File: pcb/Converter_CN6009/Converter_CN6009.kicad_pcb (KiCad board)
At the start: 2 copper layers, 45 x 22.5 mm, 15 parts, among them J1 IN+, J2 IN-, J3 OUT+, J4 OUT-

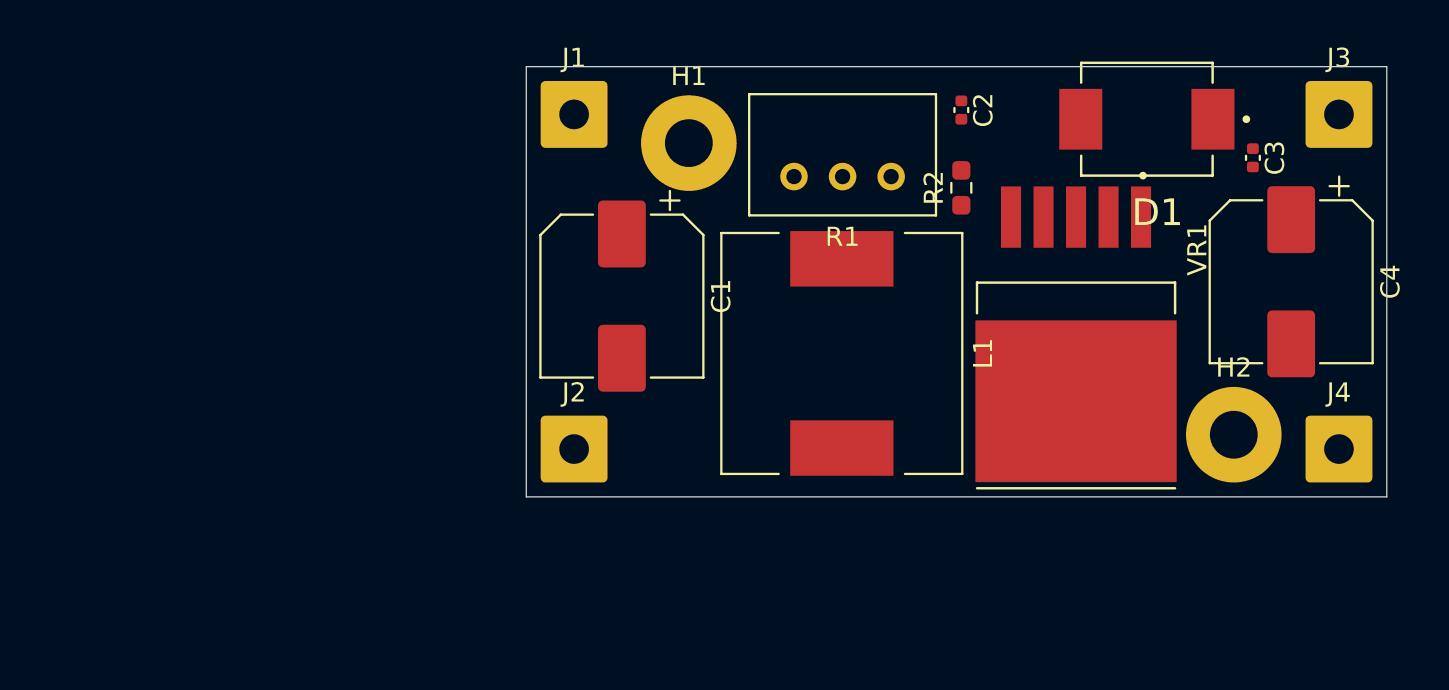
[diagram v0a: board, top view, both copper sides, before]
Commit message: se realizo ruteo de pcb y correciones
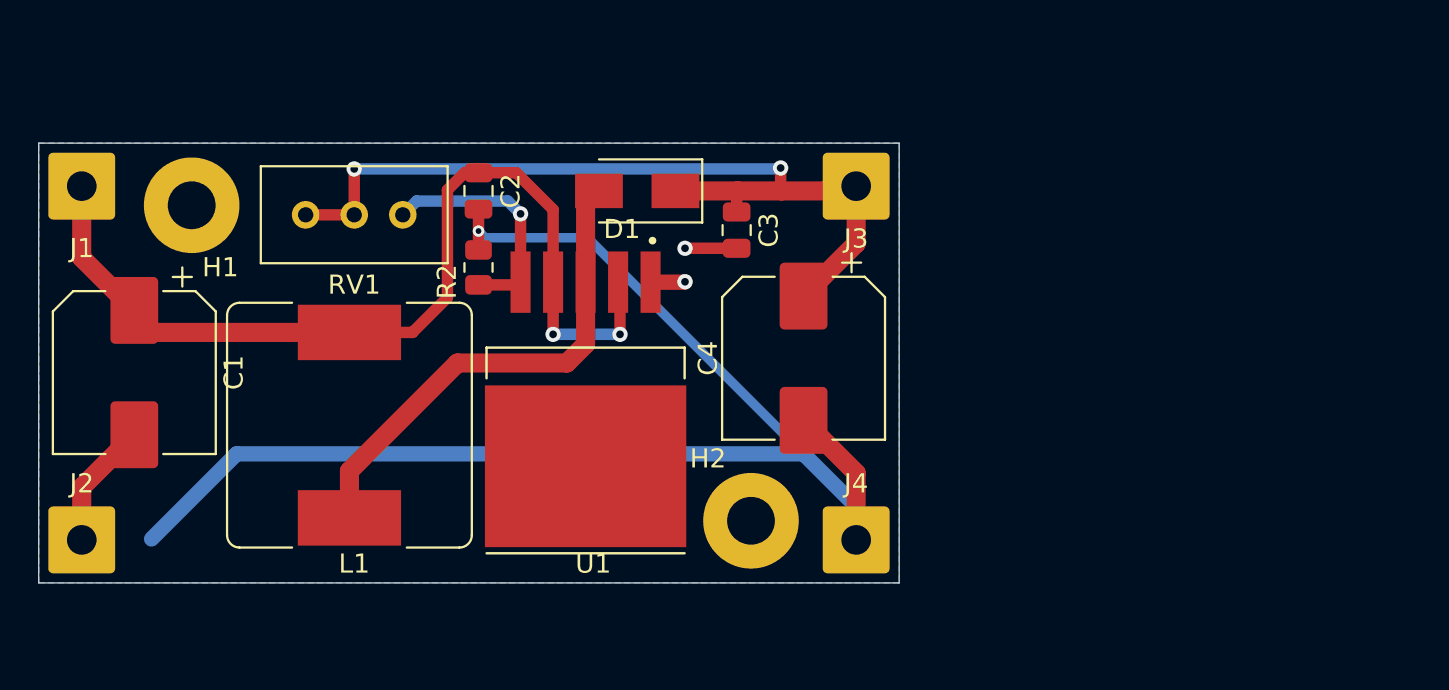
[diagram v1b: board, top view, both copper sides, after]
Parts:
- removed R1: 50K, Potentiometer_THT:Potentiometer_Bourns_3299W_Vertical
- added RV1: R_POT_TRIM, Potentiometer_THT:Potentiometer_Bourns_3296W_Vertical, F.Cu at (119.5, 88.2)
- C2, C3: footprint Capacitor_SMD:C_0402_1005Metric -> Capacitor_SMD:C_0805_2012Metric
- D1: value SS34 -> D_Schottky; footprint SS34:DIOM7959X265N -> Diode_SMD:D_SMA
- L1: footprint Inductor_SMD:L_12x12mm_H8mm -> Inductor_SMD:L_Bourns_SRR1260
- R2: footprint Resistor_SMD:R_0603_1608Metric_Pad0.98x0.95mm_HandSolder -> Resistor_SMD:R_0805_2012Metric
- moved C3 27.3 mm to (142.0, 89.0)
- moved D1 26.9 mm to (136.8, 87.0)
- moved H1 26.2 mm to (113.5, 87.8)
- moved J2 26.2 mm to (107.8, 105.2)
- moved J1 26.0 mm to (107.8, 86.8)
- moved L1 26.0 mm to (121.8, 99.2)
- moved U1 25.9 mm to (134.1, 97.9)
- moved C1 25.8 mm to (110.5, 96.5)
- moved C4 25.8 mm to (145.5, 95.8)
- moved J4 25.7 mm to (148.2, 105.2)
- moved H2 25.6 mm to (142.8, 104.2)
- moved C2 25.6 mm to (128.5, 87.0)
- moved R2 25.6 mm to (128.5, 91.0)
- moved J3 25.5 mm to (148.2, 86.8)
- renumbered VR1 to U1
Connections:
- L1 pad 2: Net-(D1-PadA) -> Net-(D1-Pad2)
- U1 pad 3: Net-(D1-PadA) -> Net-(D1-Pad2)
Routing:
- net GND: track 0.00 -> 88.0 mm, vias 0 -> 3
- net Net-(C1-Pad1): track 0.00 -> 51.0 mm, vias 0 -> 2
- net Net-(C3-Pad1): track 0.41 -> 47.4 mm, vias 0 -> 2
- net Net-(D1-Pad2): track 0.00 -> 26.2 mm
- net Net-(R2-Pad1): track 0.00 -> 12.7 mm, vias 0 -> 1
- added copper zone on B.Cu, net GND
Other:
- board size 45 x 22.5 mm -> 45 x 23 mm
- net class Default: clearance 0.8 -> 0.6
- rule trace_clearance: 0.8 -> 0.6
- board text added: "* 0,3mm agujero de via"
- board text added: "* 0,4 mm agujero de via"
- board text added: "* 0,5mm para posicionamiento de PCB"
- board text added: "* 0,6 mm pad de via"
- board text added: "* 0,6mm de margen"
- board text added: "* 0,8mm pad de via"
- board text added: "* 1mm para contorno de PCB"
- board text added: "* 1mm y 0,6mm de ancho de pista"
- board text added: "* Bottom : B.Cu"
- board text added: "* Top : F.Cu"
- board text added: "<----------- CN6009"
- board text added: "Capas"
- board text added: "DCI-FIUBA"
- board text added: "Grilla"
- board text added: "IN+"
- board text added: "IN-"
- board text added: "OUT+"
- board text added: "OUT-"
- board text added: "Replica Conversor DC-DC CN6009"
- board text added: "Tamaños seleccionados"

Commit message: se realizo todas las correcciones para la revision final
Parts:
- removed J1: IN+, Connector_Wire:SolderWire-0.75sqmm_1x01_D1.25mm_OD3.5mm
- removed J2: IN-, Connector_Wire:SolderWire-0.75sqmm_1x01_D1.25mm_OD3.5mm
- removed J3: OUT+, Connector_Wire:SolderWire-0.75sqmm_1x01_D1.25mm_OD3.5mm
- removed J4: OUT-, Connector_Wire:SolderWire-0.75sqmm_1x01_D1.25mm_OD3.5mm
- added FID1: Fiducial, Fiducial:Fiducial_0.75mm_Mask1.5mm, F.Cu at (114.2, 107.0)
- added IN+: J1, Connector_Wire:SolderWire-0.75sqmm_1x01_D1.25mm_OD3.5mm, F.Cu at (110.5, 90.5)
- added IN-: J2, Connector_Wire:SolderWire-0.75sqmm_1x01_D1.25mm_OD3.5mm, F.Cu at (110.5, 108.5)
- added OUT+: J3, Connector_Wire:SolderWire-0.75sqmm_1x01_D1.25mm_OD3.5mm, F.Cu at (150.5, 90.5)
- added OUT-: J4, Connector_Wire:SolderWire-0.75sqmm_1x01_D1.25mm_OD3.5mm, F.Cu at (150.5, 108.5)
- D1: value D_Schottky -> SS34
- RV1: value R_POT_TRIM -> 50K
- moved H1 4.45 mm to (116.2, 91.2)
- moved C1 4.30 mm to (113.0, 100.0)
- moved C2 4.30 mm to (131.0, 90.5)
- moved C3 4.30 mm to (144.5, 92.5)
- moved C4 4.30 mm to (148.0, 99.2)
- moved D1 4.30 mm to (139.3, 90.5)
- moved H2 4.30 mm to (145.2, 107.8)
- moved L1 4.30 mm to (124.2, 102.8)
- moved R2 4.30 mm to (131.0, 94.5)
- moved RV1 4.30 mm to (122.0, 91.8)
- moved U1 4.30 mm to (136.6, 101.4)
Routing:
- net GND: track 88.0 -> 72.3 mm, vias 3 -> 4
- net Net-(C3-Pad1): track 47.4 -> 45.9 mm
- added copper zone on F.Cu, net GND
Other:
- board text added: "* 0,5 mm agujero de via"
- board text added: "* 0,5 mm para posicionamiento de PCB"
- board text added: "* 0,6 mm de margen"
- board text added: "* 1 mm pad de via"
- board text added: "* 1 mm para contorno de PCB"
- board text added: "* 1mm y 0,6 mm de ancho de pista"
- board text added: "* 23 mm de ancho"
- board text added: "* 45 mm de largo"
- board text added: "Conversor DC/DC Step-Up Ajustable"
- board text added: "Diseñado en Argentina"
- board text added: "Diseño referenciado en el fabricante XLSEMI"
- board text added: "FIUBA-DCI"
- board text added: "Grilla:"
- board text added: "Tamaño de PCB:"
- board text added: "Tamaños seleccionados:"
- board text added: "Terminacion Superficial: HASL sin plomo"
- board text removed: "* 0,3mm agujero de via"
- board text removed: "* 0,4 mm agujero de via"
- board text removed: "* 0,5mm para posicionamiento de PCB"
- board text removed: "* 0,6 mm pad de via"
- board text removed: "* 0,6mm de margen"
- board text removed: "* 0,8mm pad de via"
- board text removed: "* 1mm para contorno de PCB"
- board text removed: "* 1mm y 0,6mm de ancho de pista"
- board text removed: "DCI-FIUBA"
- board text removed: "Grilla"
- board text removed: "Replica Conversor DC-DC CN6009"
- board text removed: "Tamaños seleccionados"

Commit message: ultima correccion para revision final
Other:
- board text added: "* 0,4 mm agujero de via"
- board text added: "* 0,8 mm pad de via"
